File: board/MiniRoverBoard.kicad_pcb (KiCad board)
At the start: 2 copper layers, 103.4 x 66.5 mm, 49 parts, among them J1 DEBUG, Q1 NMOS, Q2 BSS138, U2 OKI, U3 Opamp_Dual, U4 LT1910, U7 ESP32-S2-DEVKITM-1U, U8 Opamp_Dual

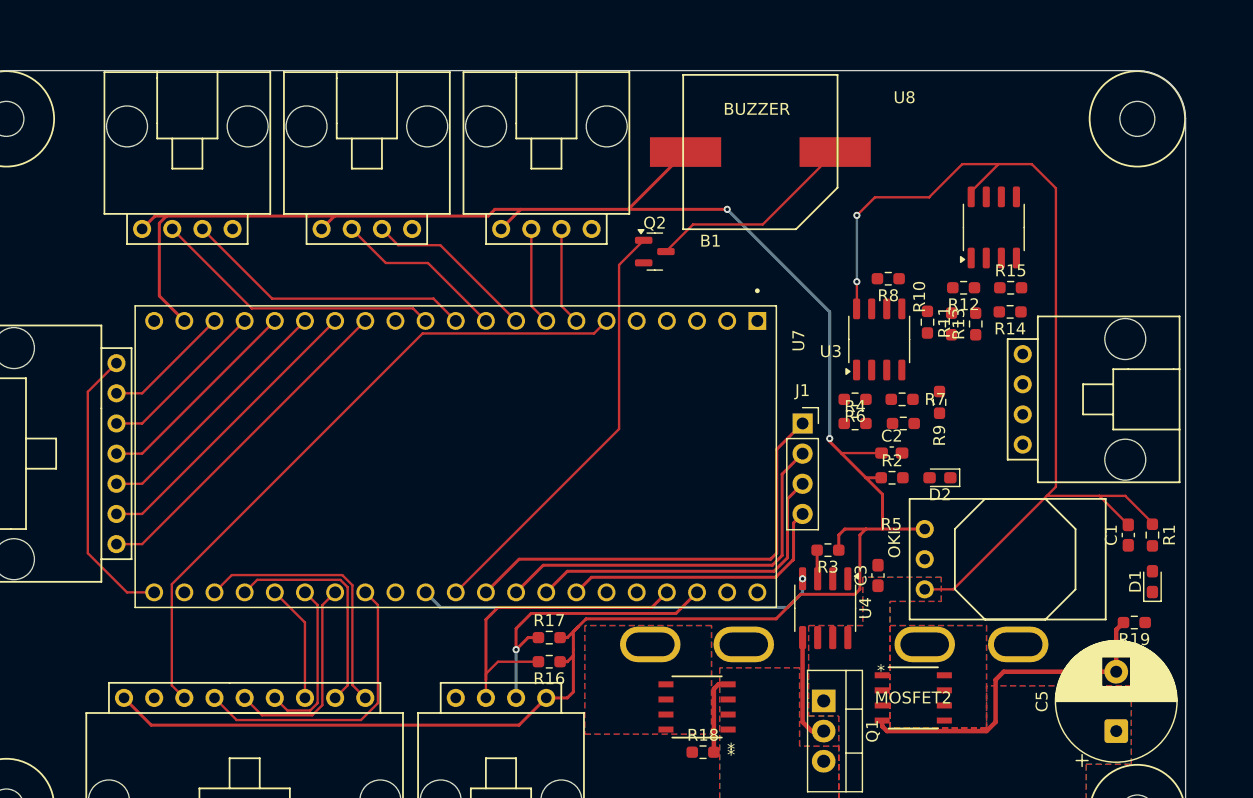
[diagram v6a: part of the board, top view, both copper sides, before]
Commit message: Move OpAmps and Changed buzzer footprint
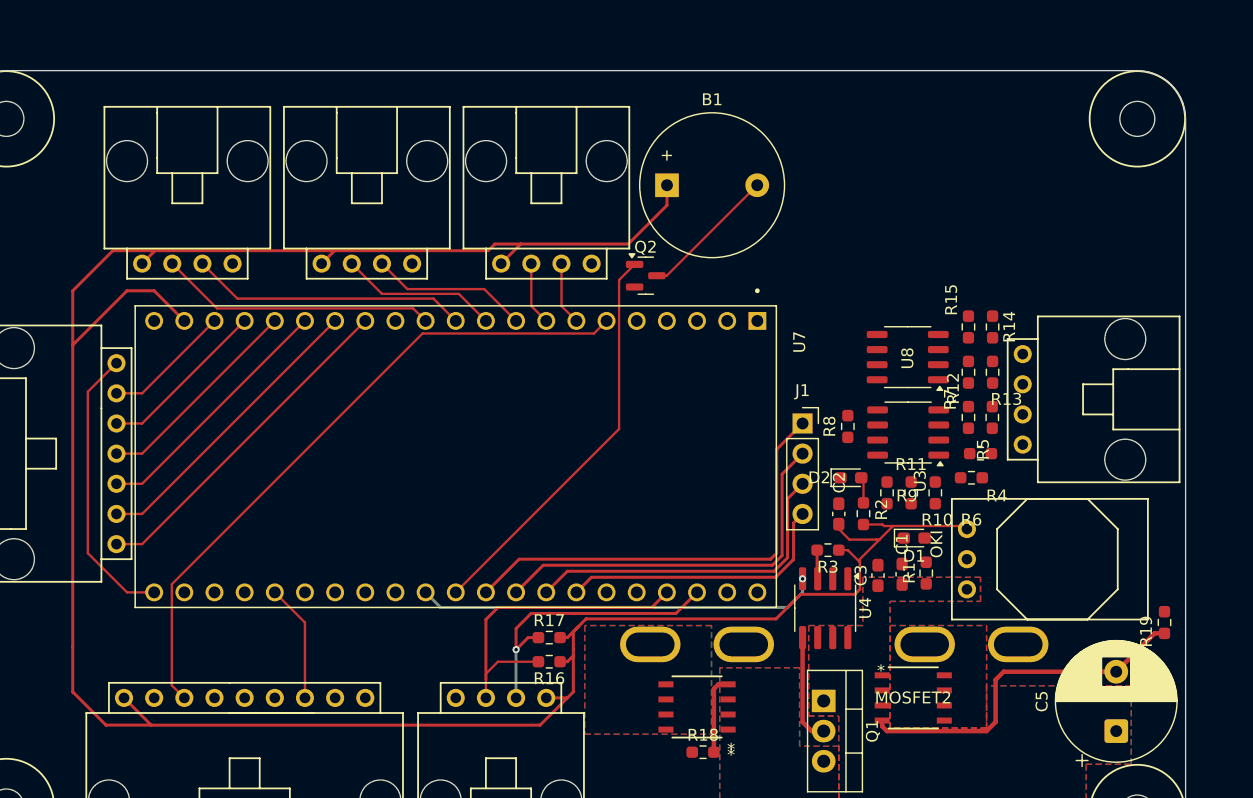
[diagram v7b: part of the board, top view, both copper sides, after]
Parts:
- B1: footprint MRDT_Devices:BUZZER_SMI_1324_TW_5V_2_R -> Buzzer_Beeper:Buzzer_12x9.5RM7.6
- moved D1 20.4 mm to (125.0, 74.2), turned to 0 degrees
- moved C1 19.3 mm to (124.0, 77.2), turned to -90 degrees
- moved R1 19.3 mm to (126.0, 77.1), turned to 90 degrees
- moved R11 14.4 mm to (124.7, 70.4)
- moved R10 14.3 mm to (126.7, 70.4)
- moved U8 13.1 mm to (124.4, 58.9), turned to 180 degrees
- moved R8 12.9 mm to (119.4, 64.8), turned to -90 degrees
- moved R6 11.8 mm to (129.8, 69.1)
- moved R4 10.9 mm to (130.6, 67.1), turned to 180 degrees
- moved R9 8.81 mm to (122.7, 70.4)
- moved U3 8.21 mm to (124.5, 65.3), turned to 180 degrees
- moved R5 7.51 mm to (131.5, 64.0), turned to 90 degrees
- moved D2 7.51 mm to (119.6, 69.1), turned to 0 degrees
- moved R12 7.12 mm to (129.5, 60.2), turned to -90 degrees
- moved C2 6.80 mm to (118.6, 72.1), turned to 90 degrees
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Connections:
- Conn2 pad 4: Net-(Conn2B-V+Log) -> (no net)
- Conn3 pad 4: Net-(Conn3B-V+Log) -> (no net)
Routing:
- net +12V: track 84.2 -> 0.00 mm, vias 2 -> 0
- net ESC_PWM_1: track 24.9 -> 0.00 mm
- net ESC_PWM_6: track 22.5 -> 0.00 mm
- net ESC_PWM_5: track 19.1 -> 0.00 mm
- net ESC_PWM_2: track 17.4 -> 0.00 mm
- net +5V: track 196.1 -> 212.0 mm, vias 2 -> 0
- net ESC_PWM_3: track 14.1 -> 0.00 mm
- net Net-(B1-V-): track 17.7 -> 11.6 mm
- net SERVO_PWN_X: track 8.27 -> 5.35 mm
- net ENCODER_PWN_X: track 8.27 -> 5.35 mm
- net Buzzer_Pin: track 36.2 -> 33.9 mm
- net Net-(D2-A): track 0.00 -> 2.19 mm
- net ENCODER_PWN_J2: track 14.5 -> 13.3 mm
- net SERVO_PWN_J3: track 24.5 -> 23.3 mm
- net SERVO_PWN_J2: track 14.5 -> 13.3 mm
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
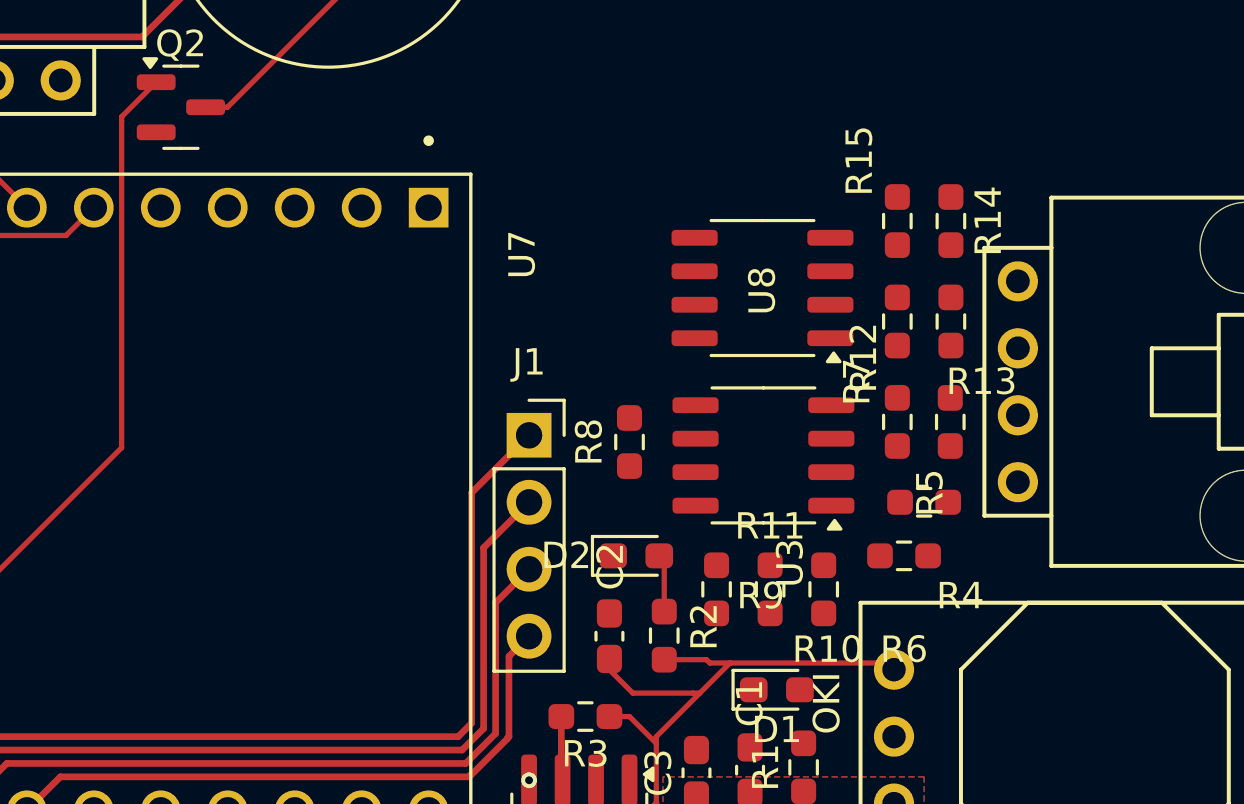
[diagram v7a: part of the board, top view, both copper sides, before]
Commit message: Add traces for OpAmps
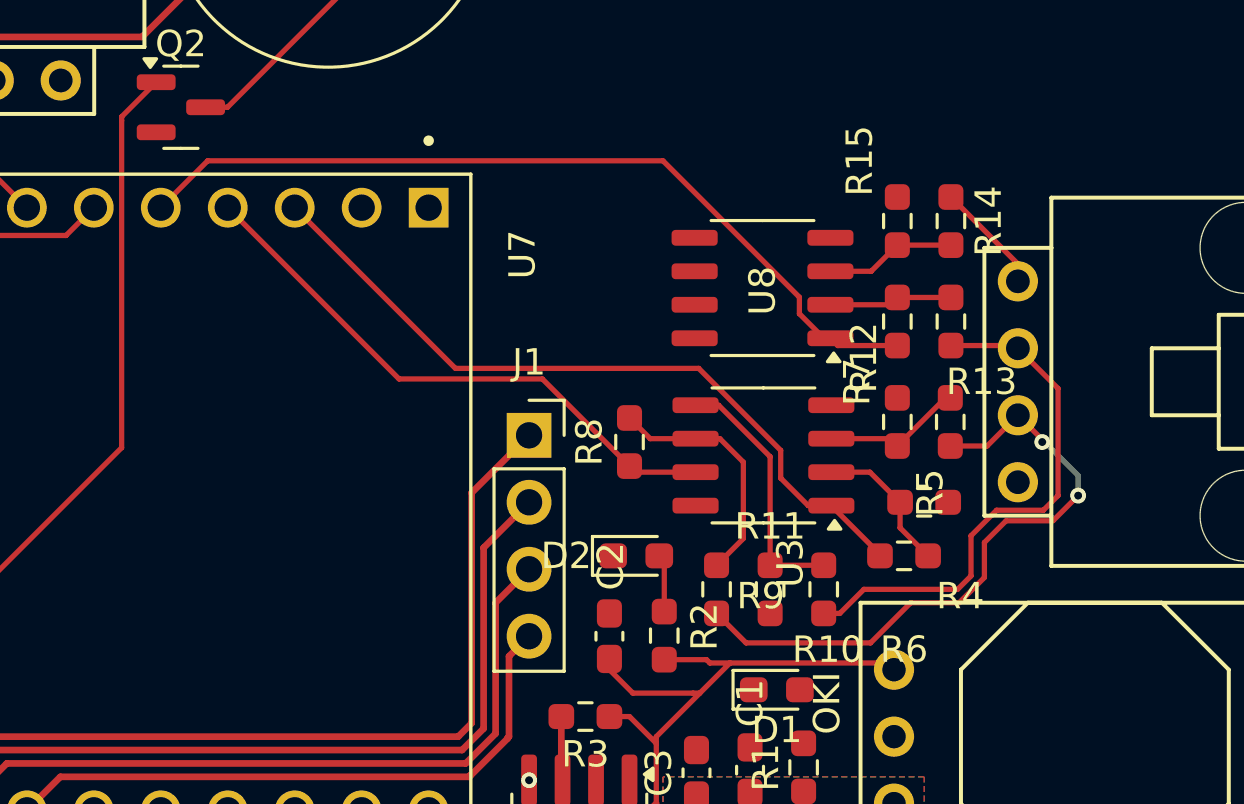
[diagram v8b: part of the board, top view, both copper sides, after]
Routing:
- net CELL_SENSE_3: track 0.00 -> 31.9 mm
- net CELL_SENSE_1: track 0.00 -> 28.3 mm
- net CELL1: track 0.00 -> 24.6 mm, vias 0 -> 2
- net CELL_SENSE_2: track 0.00 -> 21.9 mm
- net CELL2: track 0.00 -> 20.4 mm
- net Net-(U3B-+): track 0.00 -> 9.79 mm
- net Net-(U3B--): track 0.00 -> 9.35 mm
- net Net-(U3A--): track 0.00 -> 5.55 mm
- net Net-(U3A-+): track 0.00 -> 5.38 mm
- net Net-(U8A-+): track 0.00 -> 4.98 mm
- net Net-(U8A--): track 0.00 -> 4.69 mm
- net CELL3: track 0.00 -> 4.25 mm
